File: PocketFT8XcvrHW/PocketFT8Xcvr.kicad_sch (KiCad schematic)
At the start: 65 parts, among them J1 HX8357D SPI, J2 22-23-2021, J3 B5B-XH-A_LF__SN_, J4 XMT PWR, J5 HX8357D 8-BIT, Q1 2N7002DW, U1 MCP3422A1T-E/SN, U2 Si4735-D60-GU, U3 SN74ACT244DWR, U4 SI5351C-B-GM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

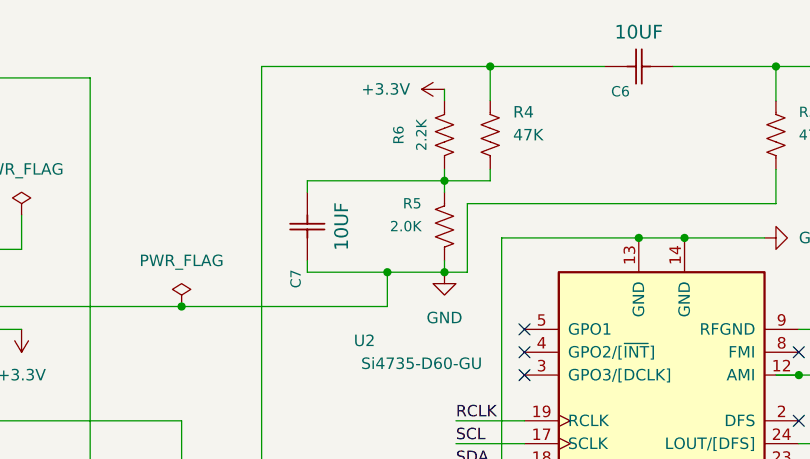
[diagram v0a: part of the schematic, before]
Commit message: Implemented SD configuration file
The config file has potential use for debugging which made it more urgent
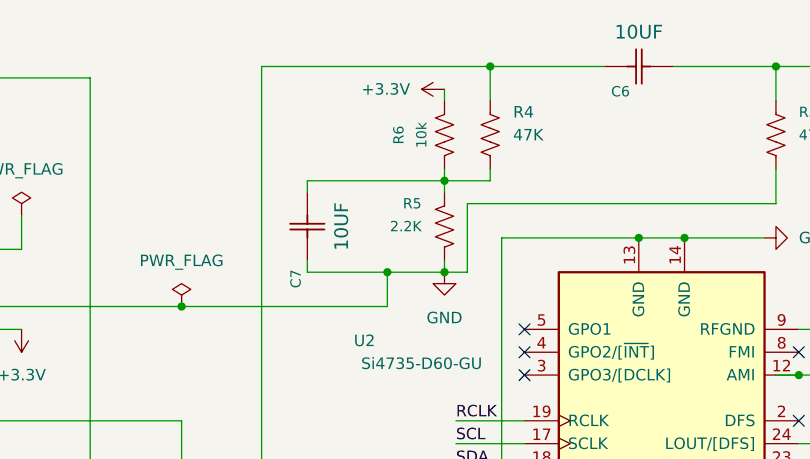
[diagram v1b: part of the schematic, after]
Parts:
- R5: value 2.0K -> 2.2K; Mfg Part # RC0603JR-072KL -> (none); PROD_ID RES-08296 -> (none)
- R6: value 2.2K -> 10k
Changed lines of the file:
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@@
 			)
 		)
-		(property "Value" "2.0K"
+		(property "Value" "2.2K"
 			(at 212.09 38.1 90)
 			(effects
@@
 			)
 		)
-		(property "Description" "RES 2K OHM 5% 1/10W 0603"
+		(property "Description" "RES 2.2K OHM 5% 1/10W 0603"
 			(at 226.06 38.1 0)
 			(effects
@@
 			)
 		)
-		(property "PROD_ID" "RES-08296"
+		(property "PROD_ID" ""
 			(at 221.488 38.1 0)
 			(effects
@@
 			)
 		)
-		(property "Mfg Part #" "RC0603JR-072KL"
+		(property "Mfg Part #" ""
 			(at 214.63 38.1 0)
 			(effects
@@
 			)
 		)
-		(property "Value" "2.2K"
+		(property "Value" "10k"
 			(at 212.09 27.94 0)
 			(effects
@@
 			)
 		)
-		(property "Description" ""
+		(property "Description" "2.2K 5% 1/10W 0603"
 			(at 226.06 27.94 0)
 			(effects

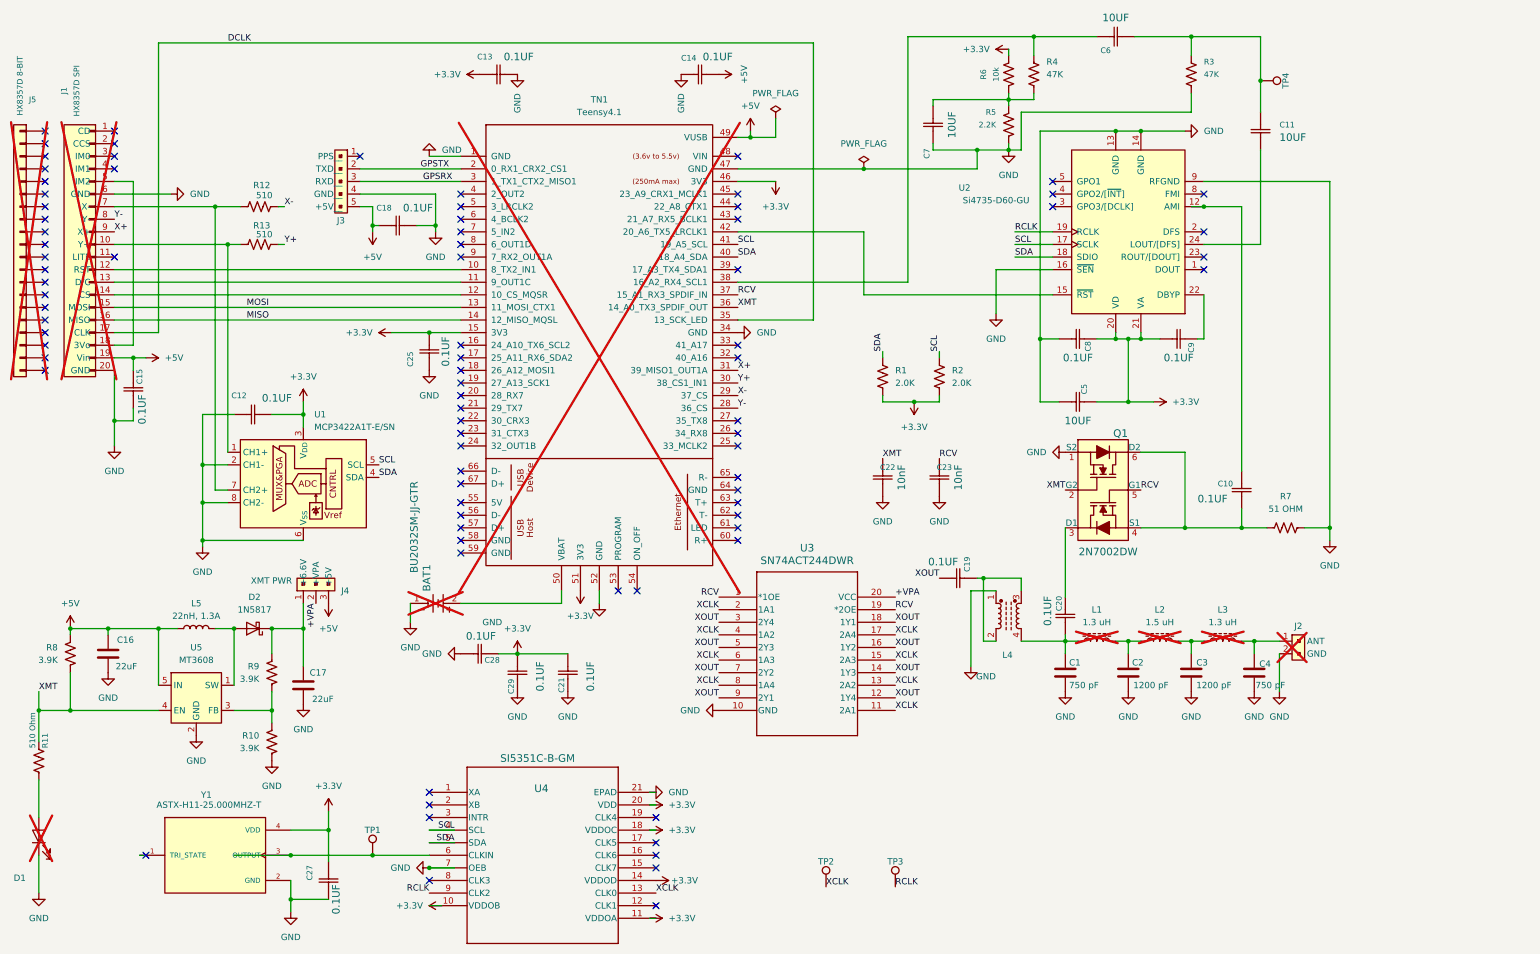
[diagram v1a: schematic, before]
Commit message: Reorganization of project for upcoming V1.10
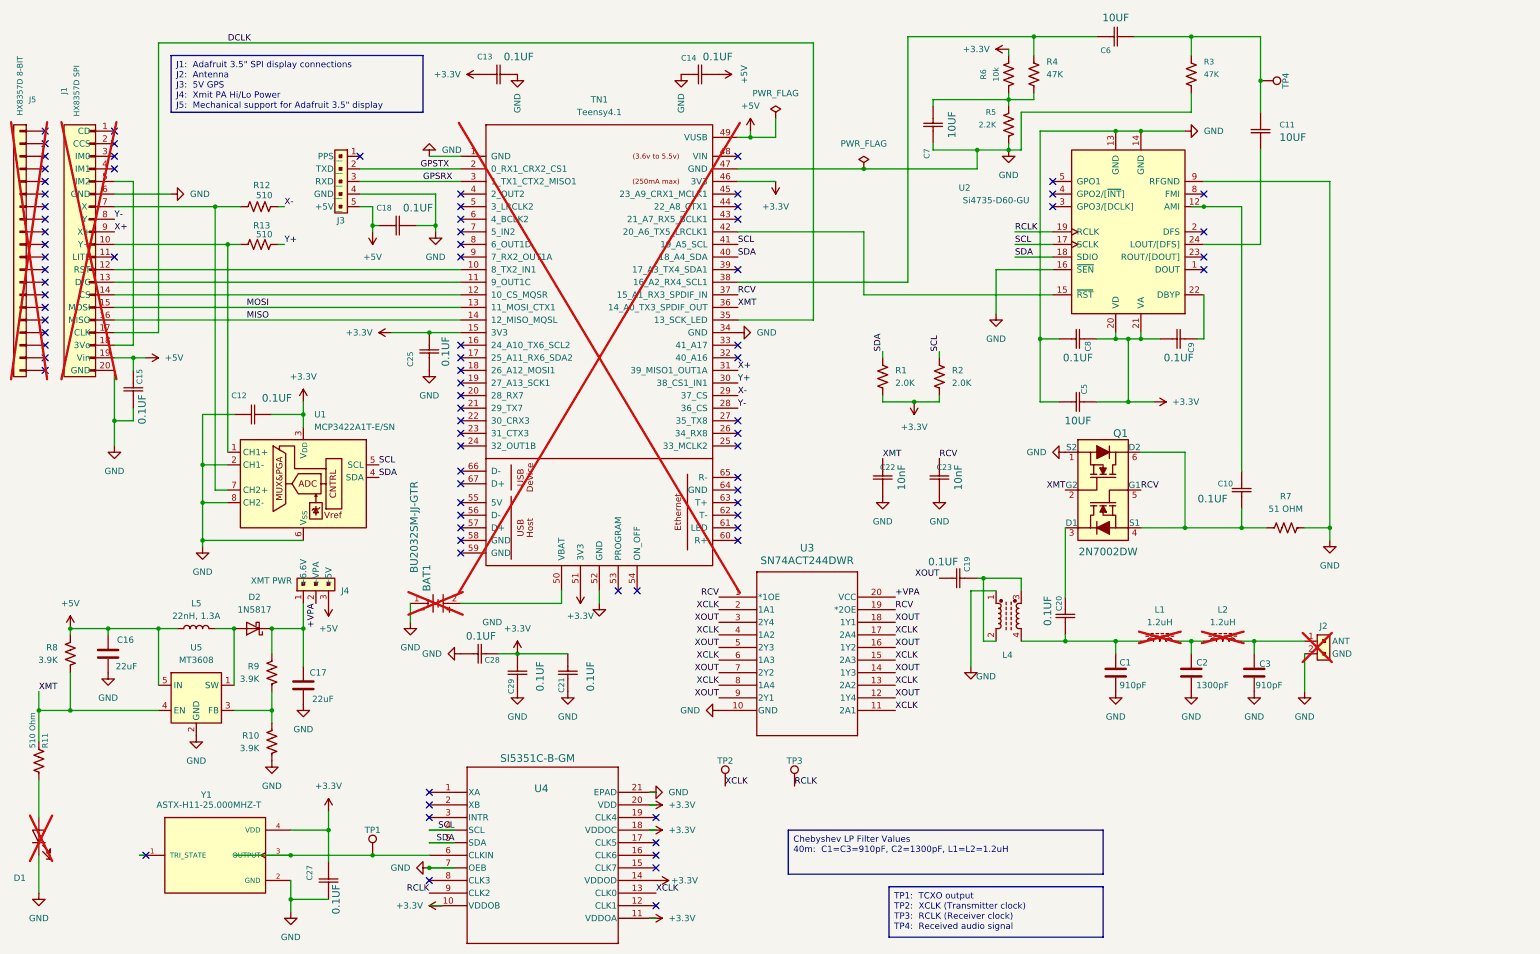
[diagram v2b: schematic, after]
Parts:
- removed C2: 1200 pF, Capacitor_SMD:C_0805_2012Metric, symbol Device:C
- removed L1: 1.3 uH, Inductor_THT:L_Toroid_Vertical_L10.0mm_W5.0mm_P5.08mm, symbol Device:L_Ferrite
- C1: value 750 pF -> 910pF
- C2: renamed from C3; value 1200 pF -> 1300pF
- C3: renamed from C4; value 750 pF -> 910pF
- L1: renamed from L2; value 1.5 uH -> 1.2uH
- L2: renamed from L3; value 1.3 uH -> 1.2uH
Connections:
- net at C1.1, C20.2, L4.4: now also L1.1
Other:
- title: Pocket FT8 Transceiver -> Idaho Edition of the Pocket FT8 Transceiver
- moved on the sheet: C1, J2, TP2, TP3

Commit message: Various debugging Issue #23 trials.
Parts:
- L5: footprint 0603 -> L_0603

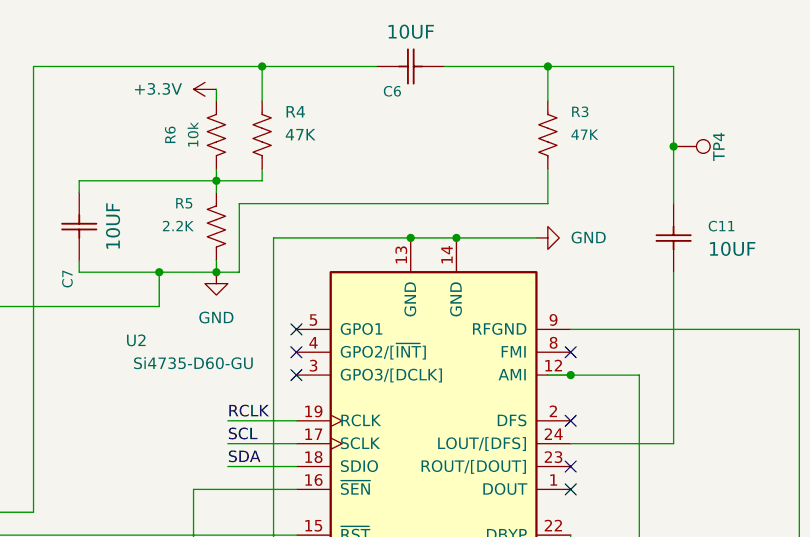
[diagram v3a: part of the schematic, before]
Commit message: Cleanup around SI4735, etc. for noise reduction
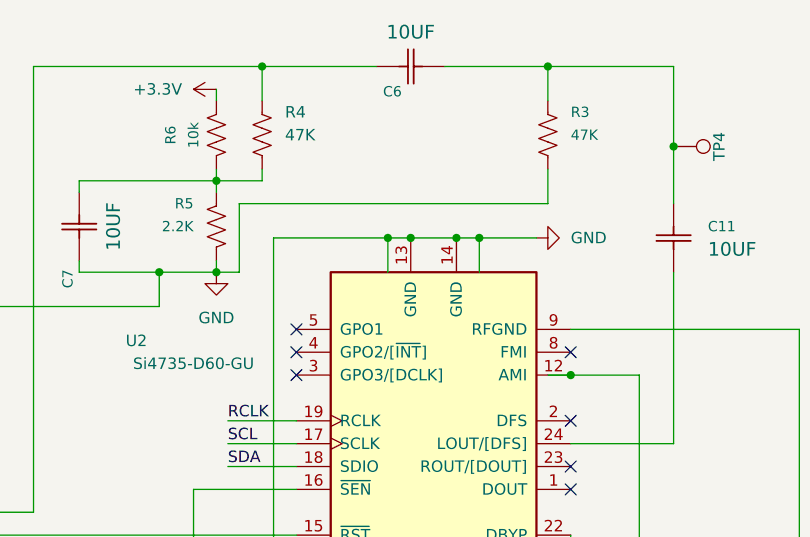
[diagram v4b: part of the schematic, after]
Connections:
- net GND: now also U2.10 (NC), U2.11 (NC)
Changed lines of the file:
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@@
 	)
 	(junction
+		(at 243.84 39.37)
+		(diameter 0)
+		(color 0 0 0 0)
+	)
+	(junction
 		(at 69.85 185.42)
 		(diameter 0)
@@
 	)
 	(junction
+		(at 233.68 39.37)
+		(diameter 0)
+		(color 0 0 0 0)
+	)
+	(junction
 		(at 72.39 139.7)
 		(diameter 0)
@@
 	(wire
 		(pts
-			(xy 250.19 39.37) (xy 241.3 39.37)
+			(xy 250.19 39.37) (xy 243.84 39.37)
 		)
 		(stroke
@@
 	(wire
 		(pts
+			(xy 233.68 39.37) (xy 233.68 43.18)
+		)
+		(stroke
+			(width 0)
+			(type default)
+		)
+	)
+	(wire
+		(pts
 			(xy 214.63 33.02) (xy 214.63 34.29)
 		)
@@
 	(wire
 		(pts
+			(xy 243.84 39.37) (xy 243.84 43.18)
+		)
+		(stroke
+			(width 0)
+			(type default)
+		)
+	)
+	(wire
+		(pts
 			(xy 43.18 21.59) (xy 43.18 80.01)
 		)
@@
 	(wire
 		(pts
+			(xy 233.68 39.37) (xy 236.22 39.37)
+		)
+		(stroke
+			(width 0)
+			(type default)
+		)
+	)
+	(wire
+		(pts
 			(xy 69.85 190.5) (xy 69.85 194.31)
 		)
@@
 	(wire
 		(pts
+			(xy 243.84 39.37) (xy 241.3 39.37)
+		)
+		(stroke
+			(width 0)
+			(type default)
+		)
+	)
+	(wire
+		(pts
 			(xy 54.61 111.76) (xy 54.61 54.61)
 		)
@@
 	(wire
 		(pts
-			(xy 220.98 39.37) (xy 236.22 39.37)
+			(xy 220.98 39.37) (xy 233.68 39.37)
 		)
 		(stroke
@@
 			)
 		)
-		(property "Description" "RF RX AM/FM 153KHZ-279KHZ 24SSOP"
+		(property "Description" "AM/FM/SW/LW Broadcast Radio Receiver with RDS/RBDS"
 			(at 238.76 59.69 0)
 			(effects

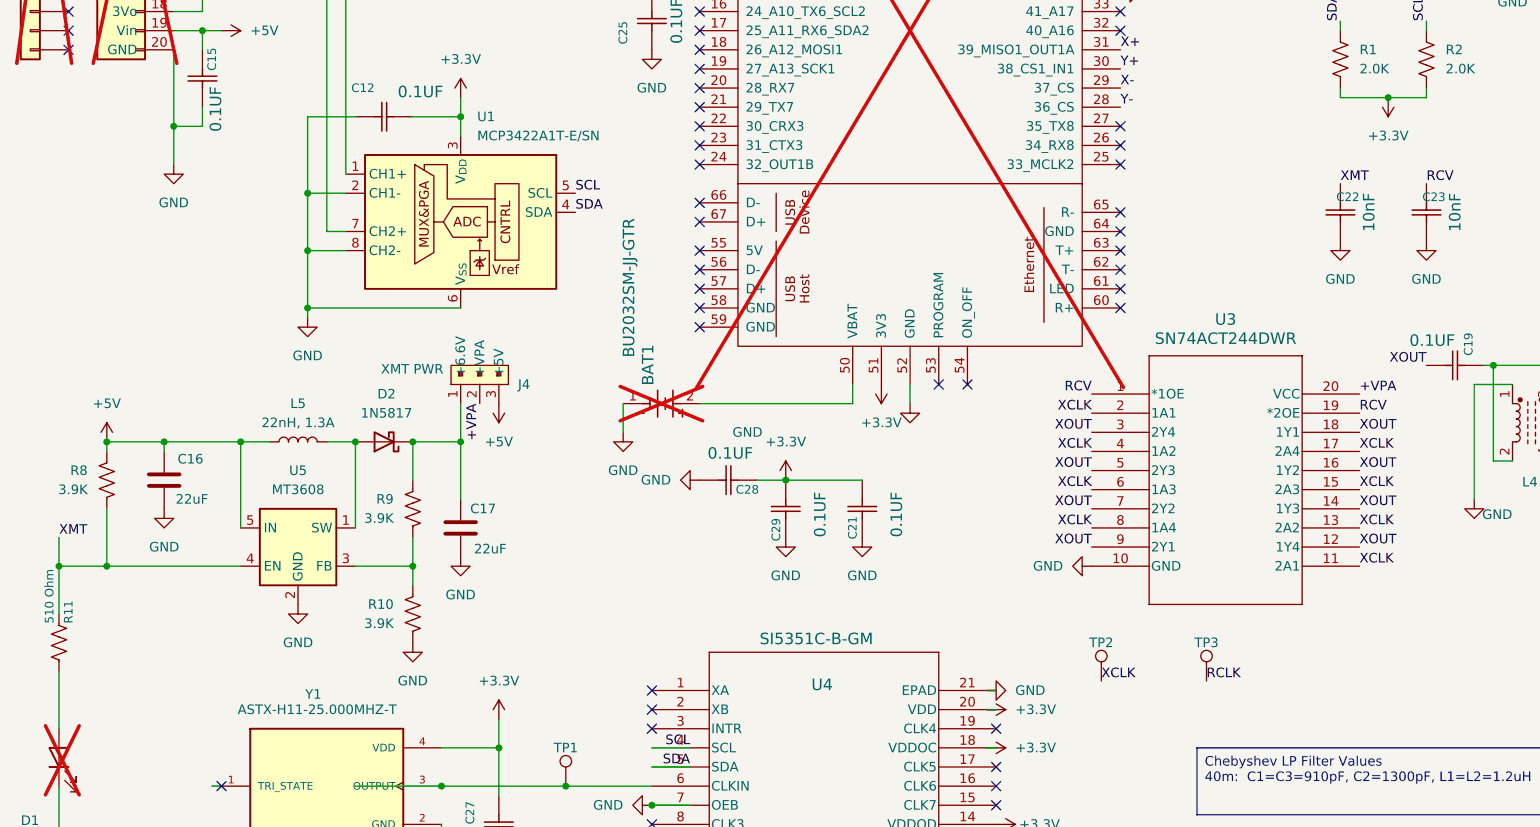
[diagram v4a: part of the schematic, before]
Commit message: Removed unobtainium MT3608
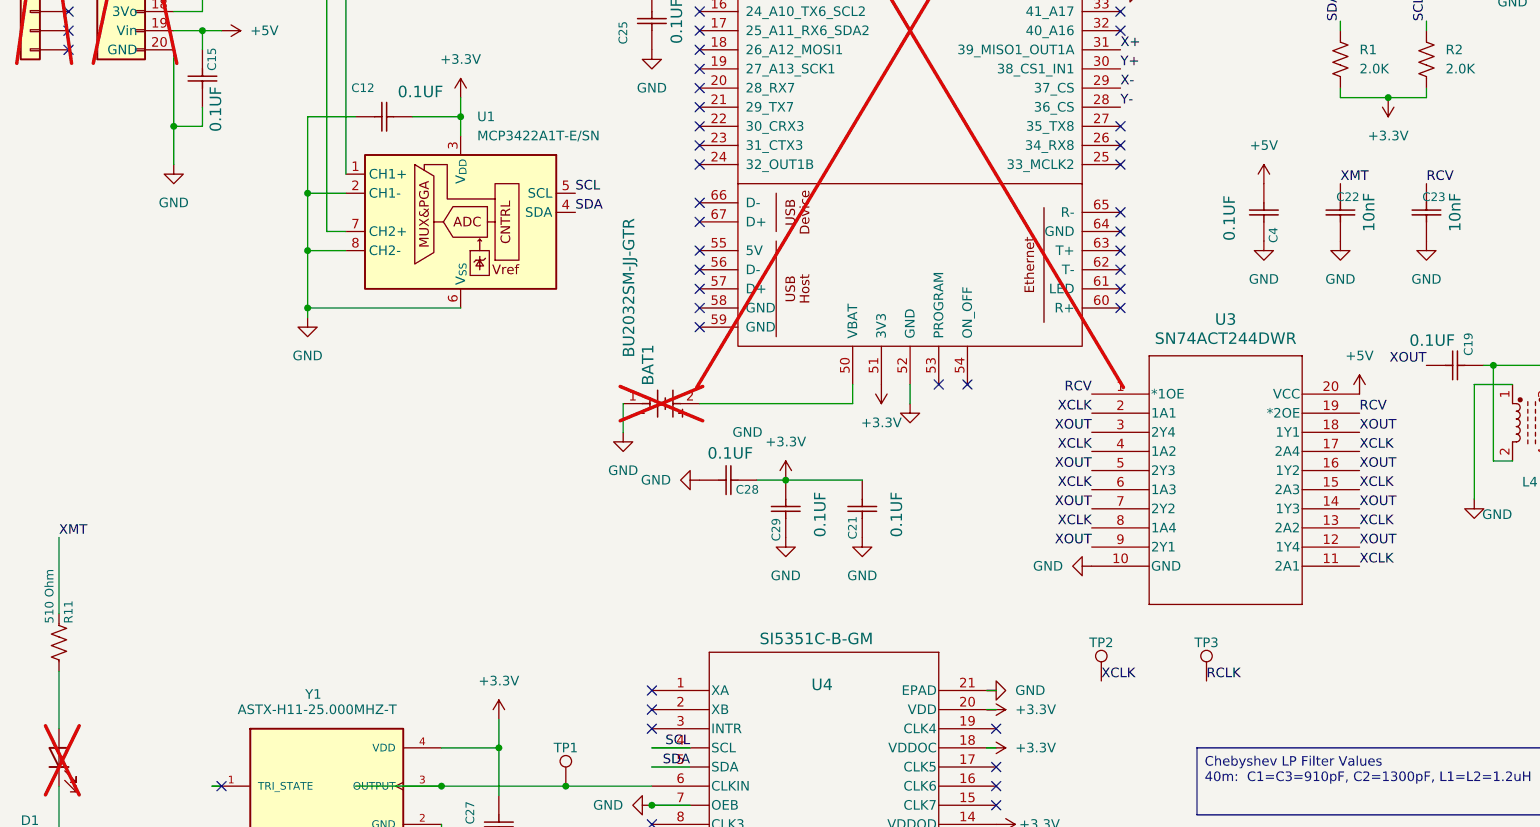
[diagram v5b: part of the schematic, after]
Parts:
- removed C16, C17: 22uF, 0603, symbol SparkFun-Capacitor:C
- removed D2: 1N5817, 1N5817T:DO-41_DIO, symbol Device:D_Schottky
- removed J4: XMT PWR, digikey-footprints:PinHeader_1x3_P2.54mm_Drill1.02mm, symbol dk_Rectangular-Connectors-Headers-Male-Pins:0022232031
- removed L5: 22nH, 1.3A, L_0603, symbol SparkFun-Coil:L
- removed R10, R8, R9: 3.9K, Resistor_SMD:R_0603_1608Metric, symbol SparkFun-Resistor:2.0k_0603
- removed U5: MT3608, Package_TO_SOT_SMD:SOT-23-6, symbol Regulator_Switching:MT3608
- added C4: 0.1UF, Capacitor_SMD:C_0603_1608Metric, symbol Kemet2024-08-02_22-05-35:C0603C104K4RACTU
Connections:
- net +VPA is gone; now on net +5V: U3.20 (VCC)
- net +5V: now also C4.2
- net GND: now also C4.1
